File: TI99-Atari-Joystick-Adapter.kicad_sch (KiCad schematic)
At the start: 13 parts, among them J1 DE9_Plug_MountingHoles, J2 DE9_Plug_MountingHoles, J3 DE9_Receptacle_MountingHoles

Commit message: Initial Design v0.01
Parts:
- added H1, H2, H3, H4: MountingHole, MountingHole:MountingHole_2.5mm, symbol Mechanical:MountingHole

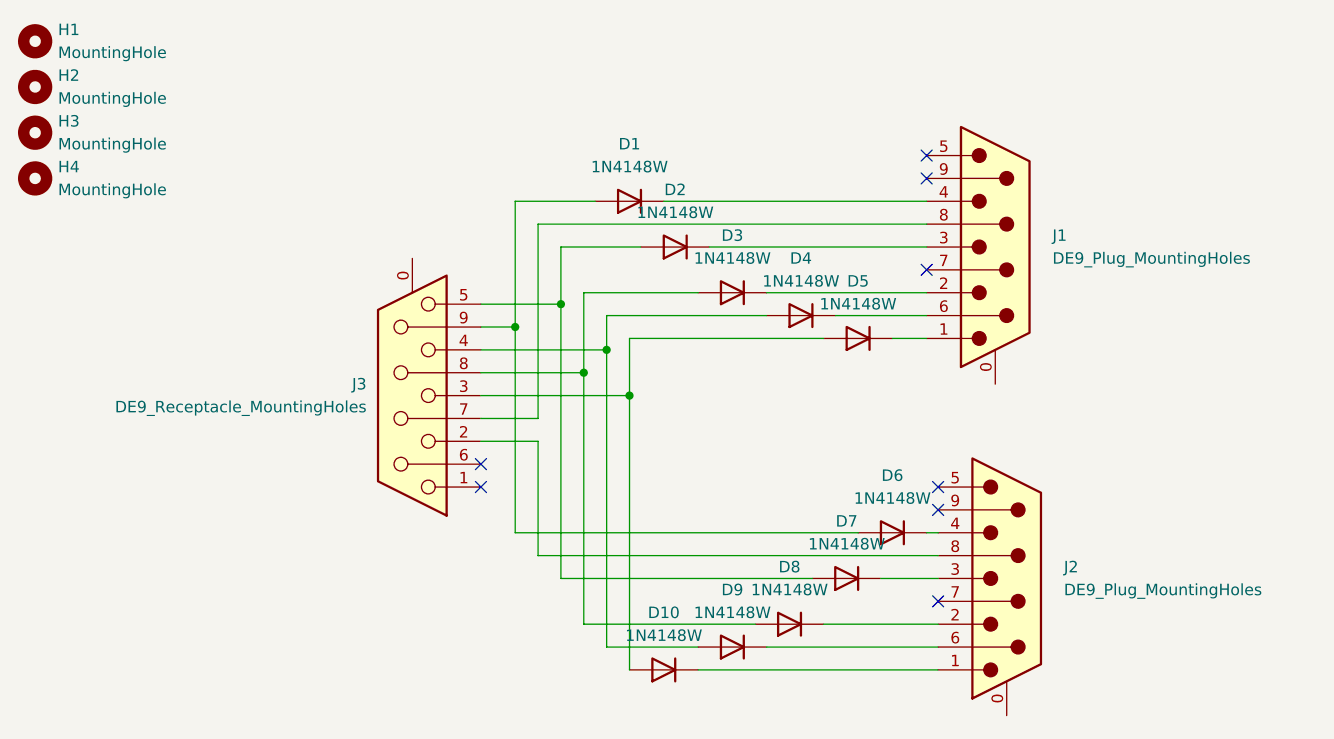
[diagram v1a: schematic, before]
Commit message: Update board size, add tracks & vias and board image.
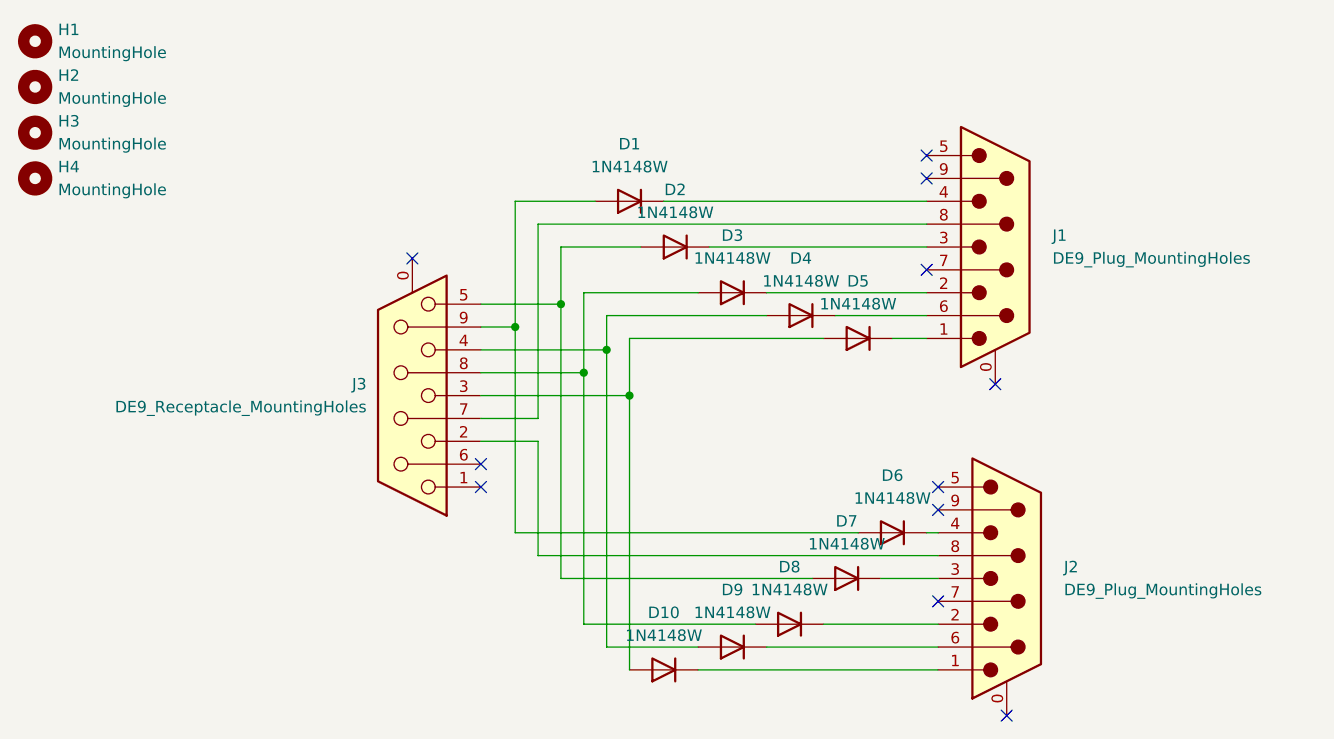
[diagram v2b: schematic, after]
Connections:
- no-connect marks 8 -> 11
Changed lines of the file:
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@@
+	)
+	(no_connect
+		(at 76.2 72.39)
 	)
 	(no_connect
@@
 	)
 	(no_connect
+		(at 140.97 86.36)
+	)
+	(no_connect
 		(at 133.35 73.66)
 	)
@@
 		(at 134.62 110.49)
 	)
+	(no_connect
+		(at 142.24 123.19)
+	)
 	(wire
